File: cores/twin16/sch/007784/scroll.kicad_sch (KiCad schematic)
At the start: 90 parts, among them J1 A4H, J53 FDN, J60 R8B, J66 N8B, J75 N2B, J78 N2P, J81 R2N, K1 A4H, K80 R2P, M1 FDN, M15 FDN, M22 FDN, M29 FDN, M36 FDN, M43 FDN, M50 FDN, M57 FDN, M64 FDN, M71 FDN, M8 FDN, P1 A4H, P51 R8B, P57 FDN, P64 FDN, P71 FDN, P78 N2P, Q29 FDN, Q57 N2B, Q8 FDN

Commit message: The counter H2 is connected to FDO Q69, not counter /H2 as it was previously. The flip flop D78 for BEFLAG was incorrectly clocked, it is now clocked by the counter value for word 0 in.
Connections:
- net at J78.: now also J75.; no longer J60.
- net at O80.: now also L78.; no longer O79.
- net at P78.: now also Q57.; no longer O80.
- net at K80.: now also J81.; no longer J78.
- net at J81.: now also H79.; no longer K80.
- new net: F28. (~{R}), F70. (~{R}), F78. (~{R}), F86. (~{R}), G82. (~{R}), G82. (~{R}), G82. (~{R}), G82. (~{R}), R63.
- new net: E28. (S4), F70. (~{R})
- new net: F70. (~{R}), F70. (~{R}), F70. (~{R}), F70. (~{R}), F70. (~{R}), F70. (~{R}), F70. (~{R}), F70. (~{R}), R59.
- new net: F70. (~{R}), I21. (S4) (x4)
- new net: F70. (~{R}), F70. (~{R}), F70. (~{R}), F70. (~{R}), F70. (~{R}), F70. (~{R}), F70. (~{R}), F70. (~{R}), R17.
- new net: F70. (~{R}), P1. (S4) (x8)
- new net: J60., J78.
- new net: G21. (S4), G82. (~{R}) (x4)
- new net: E28. (S4), G21. (S4)
- new net: G21. (S4), J1. (S4)
- new net: E28. (S4), F78. (~{R})
- new net: O79., O80.
- new net: O80., P78.
- new net: L71. (~{R}), L71. (~{R}), L71. (~{R}), L71. (~{R}), L71. (~{R}), L71. (~{R}), L71. (~{R}), L71. (~{R}), R21.
- new net: J1. (S4), L71. (~{R}) (x4)
- new net: F70. (~{R}), K1. (S4) (x4)
- new net: J78., K80.
- new net: K1. (S4), L71. (~{R}) (x4)
- new net: P51., P78.
- new net: K80., L78.
- new net: E28. (S4), F28. (~{R})
- new net: J66., J81.
- new net: E28. (S4), F86. (~{R})
- new net: I21. (S4), P1. (S4)
- new net: P1. (S4), P1. (S4)
- new net: I21. (S4), K1. (S4)
- new net: J1. (S4), K1. (S4)
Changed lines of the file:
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@@
   (title_block
     (title "Konami 007784")
-    (date "2023-09-11")
+    (date "2023-10-23")
   )
   (junction (at 218.44 53.34) (diameter 0) (color 0 0 0 0)

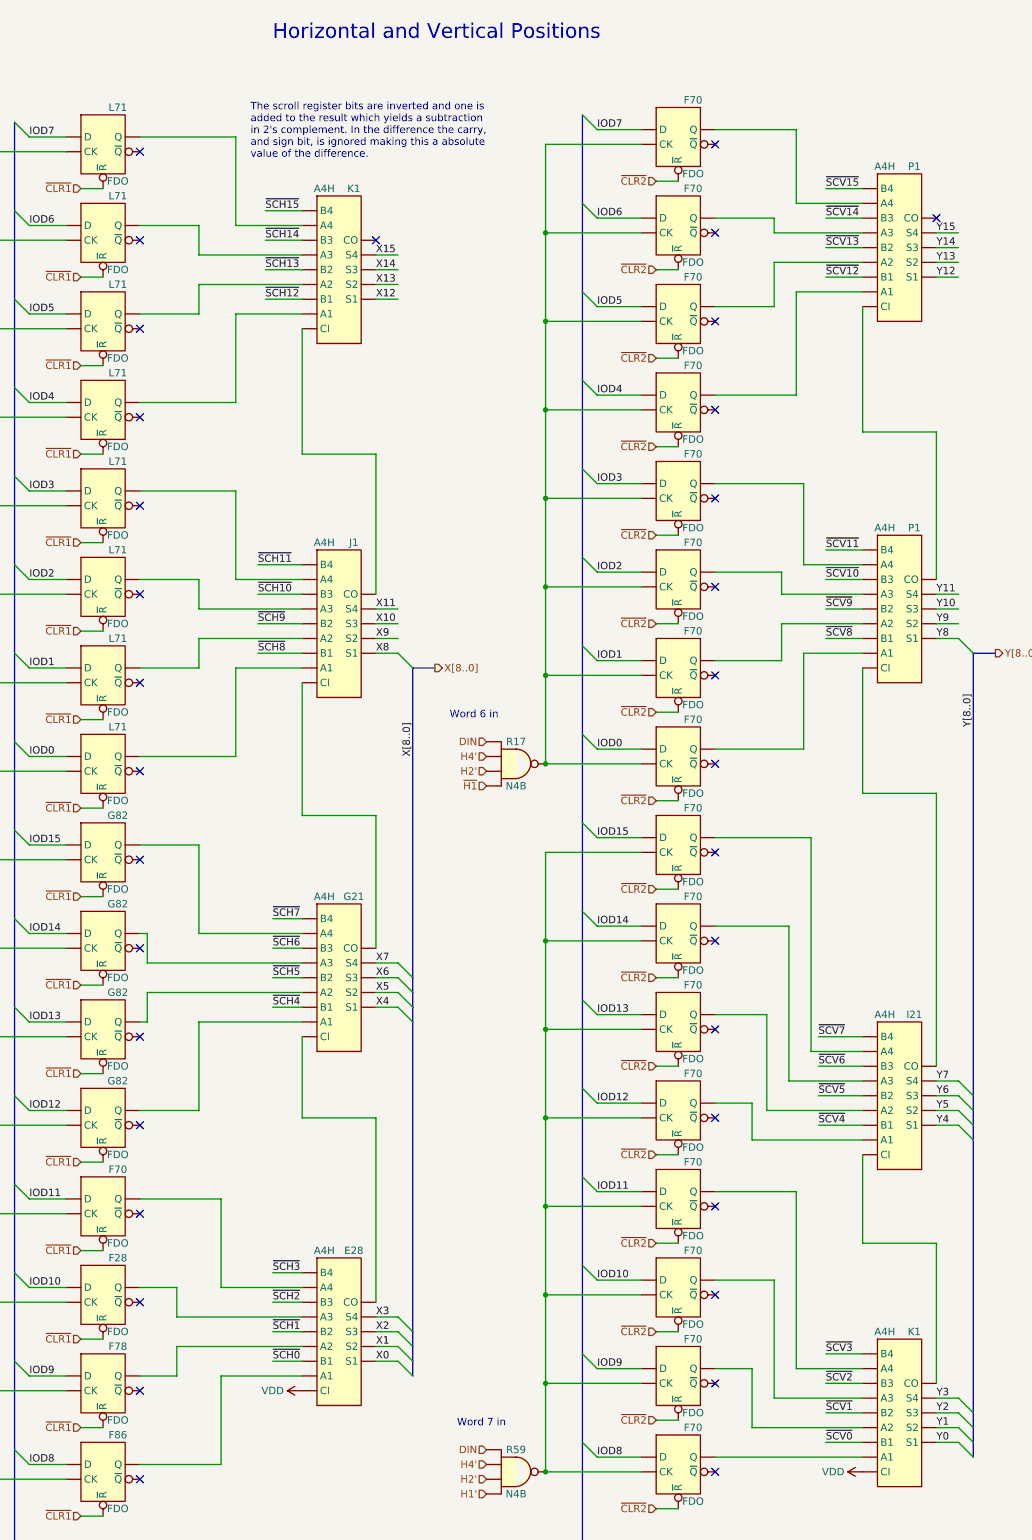
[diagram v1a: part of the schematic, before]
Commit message: updated references to jtkicad libraries
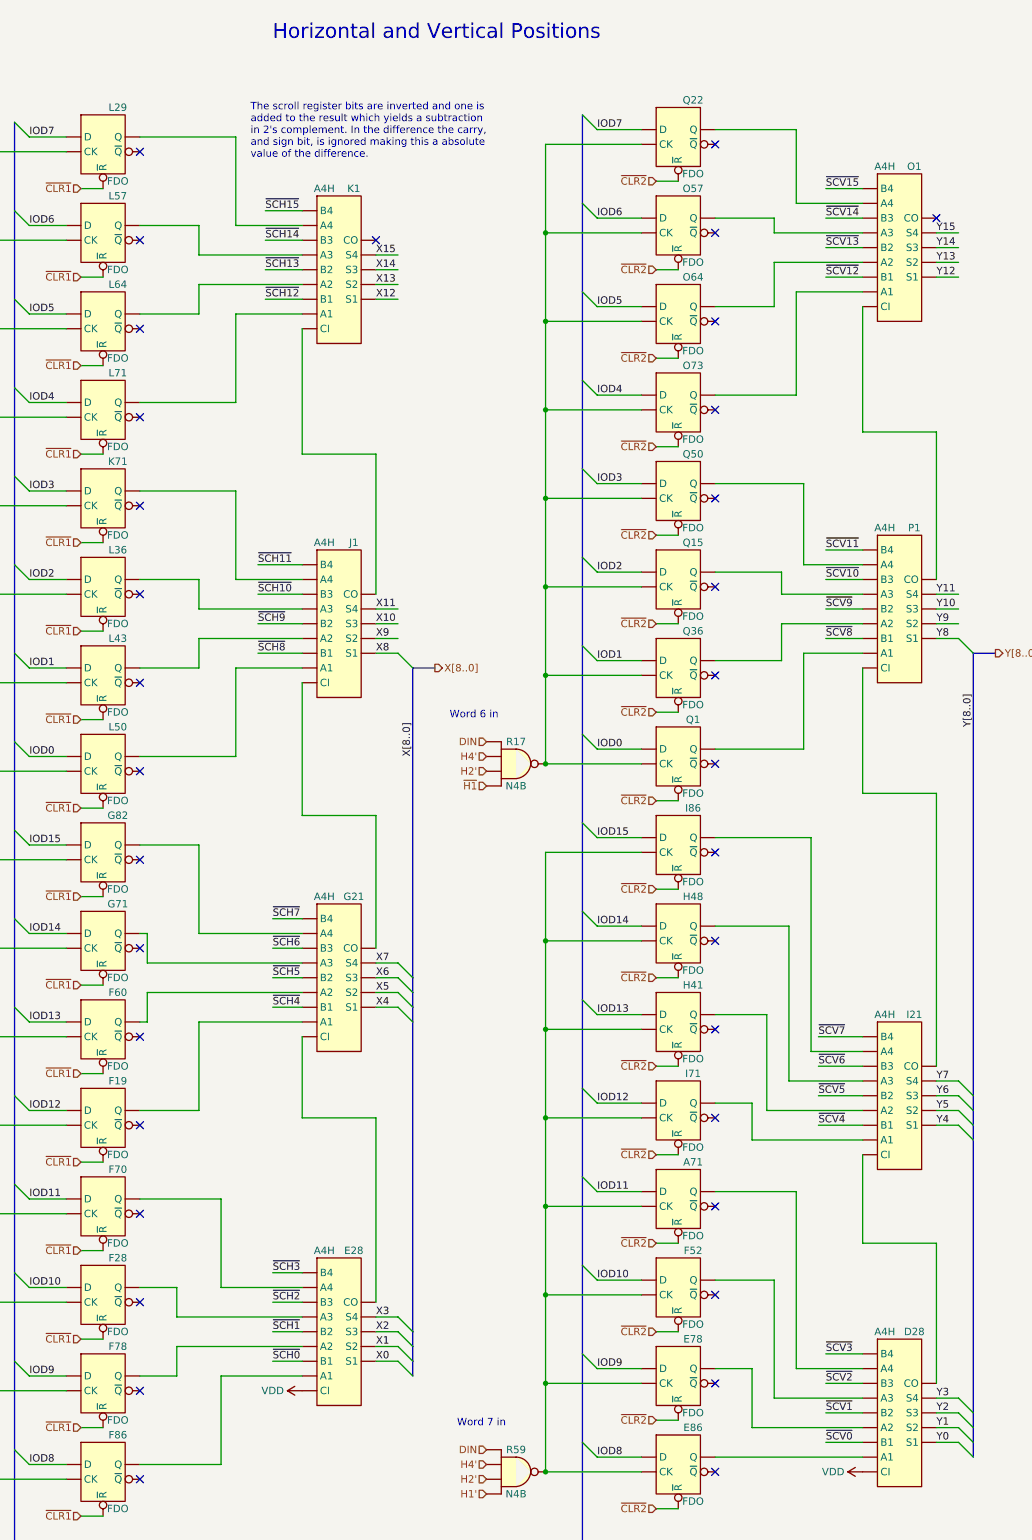
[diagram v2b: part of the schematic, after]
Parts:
- A71, E78, E86, F52, H41, H48, I71, I86, O57, O64, O73, Q1, Q15, Q22, Q36, Q50: renamed from F70; symbol fujitsu-av:FDO -> ga_fujitsu_av:FDO
- D28: renamed from K1; symbol fujitsu-av:A4H -> ga_fujitsu_av:A4H
- E28, G21, I21, J1, K1, P1: symbol fujitsu-av:A4H -> ga_fujitsu_av:A4H
- F19, F60, G71: renamed from G82; symbol fujitsu-av:FDO -> ga_fujitsu_av:FDO
- F28, F70, F78, F86, G82, L71: symbol fujitsu-av:FDO -> ga_fujitsu_av:FDO
- H79, J81: symbol fujitsu-av:R2N -> ga_fujitsu_av:R2N
- J53, L1, L15, L22, L8, M1, M15, M22, M29, M36, M43, M50, M57, M64, M71, M8, N1, N15, N22, N29, N36, N43, N50, N57, N64, N71, N8, P57, P64, P71, Q29, Q8: symbol fujitsu-av:FDN -> ga_fujitsu_av:FDN
- J60, P51: symbol fujitsu-av:R8B -> ga_fujitsu_av:R8B
- J66, O51: symbol fujitsu-av:N8B -> ga_fujitsu_av:N8B
- J75, Q57: symbol fujitsu-av:N2B -> ga_fujitsu_av:N2B
- J78, L78, P78: symbol fujitsu-av:N2P -> ga_fujitsu_av:N2P
- K71, L29, L36, L43, L50, L57, L64: renamed from L71; symbol fujitsu-av:FDO -> ga_fujitsu_av:FDO
- K80, O80: symbol fujitsu-av:R2P -> ga_fujitsu_av:R2P
- O1: renamed from P1; symbol fujitsu-av:A4H -> ga_fujitsu_av:A4H
- O79: symbol fujitsu-av:V1N -> ga_fujitsu_av:V1N
- R17, R21, R59, R63: symbol fujitsu-av:N4B -> ga_fujitsu_av:N4B
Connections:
- net at J78.: now also J75.; no longer J60.
- net at O80.: now also L78.; no longer O79.
- net at P78.: now also Q57.; no longer O80.
- net at K80.: now also J81.; no longer J78.
- net at J81.: now also H79.; no longer K80.
- new net: F19. (~{R}), F28. (~{R}), F60. (~{R}), F70. (~{R}), F78. (~{R}), F86. (~{R}), G71. (~{R}), G82. (~{R}), R63.
- new net: E28. (S4), F70. (~{R})
- new net: A71. (~{R}), E78. (~{R}), E86. (~{R}), F52. (~{R}), H41. (~{R}), H48. (~{R}), I71. (~{R}), I86. (~{R}), R59.
- new net: I21. (S4), I71. (~{R})
- new net: O57. (~{R}), O64. (~{R}), O73. (~{R}), Q1. (~{R}), Q15. (~{R}), Q22. (~{R}), Q36. (~{R}), Q50. (~{R}), R17.
- new net: P1. (S4), Q36. (~{R})
- new net: J60., J78.
- new net: F19. (~{R}), G21. (S4)
- new net: E28. (S4), G21. (S4)
- new net: G21. (S4), G82. (~{R})
- new net: F60. (~{R}), G21. (S4)
- new net: G21. (S4), G71. (~{R})
- new net: G21. (S4), J1. (S4)
- new net: E28. (S4), F78. (~{R})
- new net: O1. (S4), O57. (~{R})
- new net: O79., O80.
- new net: O80., P78.
- new net: K71. (~{R}), L29. (~{R}), L36. (~{R}), L43. (~{R}), L50. (~{R}), L57. (~{R}), L64. (~{R}), L71. (~{R}), R21.
- new net: J1. (S4), L50. (~{R})
- new net: J1. (S4), L43. (~{R})
- new net: A71. (~{R}), D28. (S4)
- new net: J78., K80.
- new net: H41. (~{R}), I21. (S4)
- new net: K1. (S4), L64. (~{R})
- new net: P1. (S4), Q50. (~{R})
- new net: K1. (S4), L57. (~{R})
- new net: D28. (S4), E86. (~{R})
- new net: P51., P78.
- new net: K80., L78.
- new net: E28. (S4), F28. (~{R})
- new net: K1. (S4), L71. (~{R})
- new net: D28. (S4), F52. (~{R})
- new net: J66., J81.
- new net: E28. (S4), F86. (~{R})
- new net: P1. (S4), Q15. (~{R})
- new net: P1. (S4), Q1. (~{R})
- new net: J1. (S4), K71. (~{R})
- new net: O1. (S4), O64. (~{R})
- new net: K1. (S4), L29. (~{R})
- new net: I21. (S4), P1. (S4)
- new net: O1. (S4), P1. (S4)
- new net: I21. (S4), I86. (~{R})
- new net: D28. (S4), E78. (~{R})
- new net: O1. (S4), Q22. (~{R})
- new net: D28. (S4), I21. (S4)
- new net: O1. (S4), O73. (~{R})
- new net: J1. (S4), L36. (~{R})
- new net: H48. (~{R}), I21. (S4)
- new net: J1. (S4), K1. (S4)

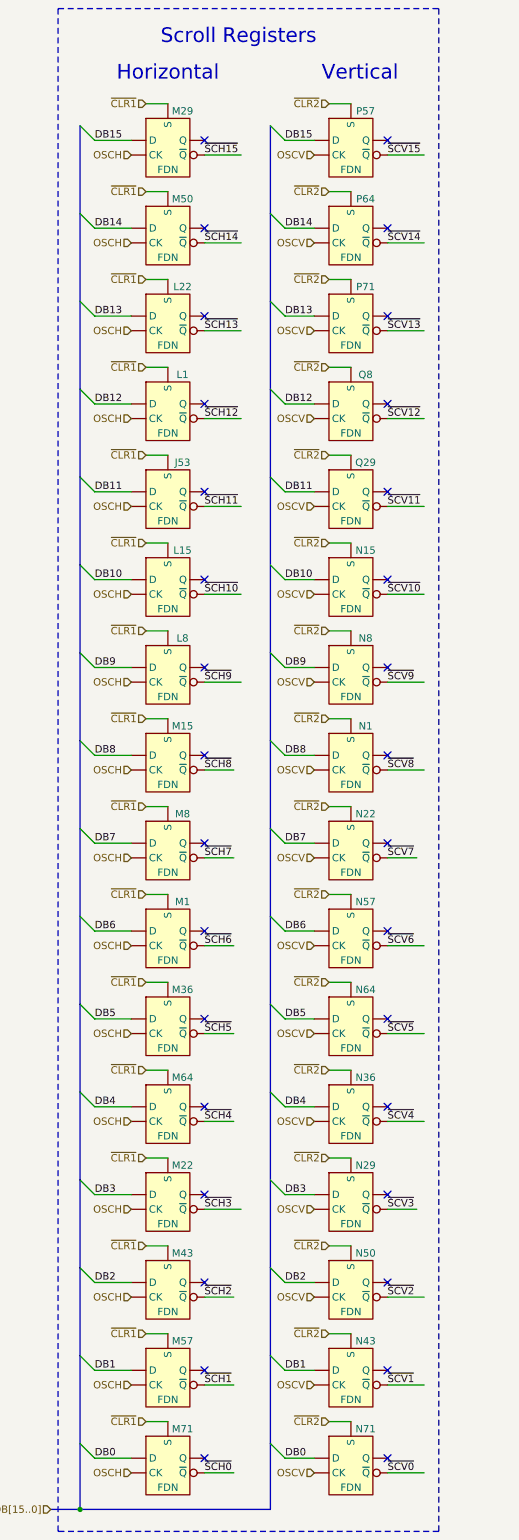
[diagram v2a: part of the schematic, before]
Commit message: changed symbol FDN to active low symbol. Updated to correct name for OKI Gate Arrays.
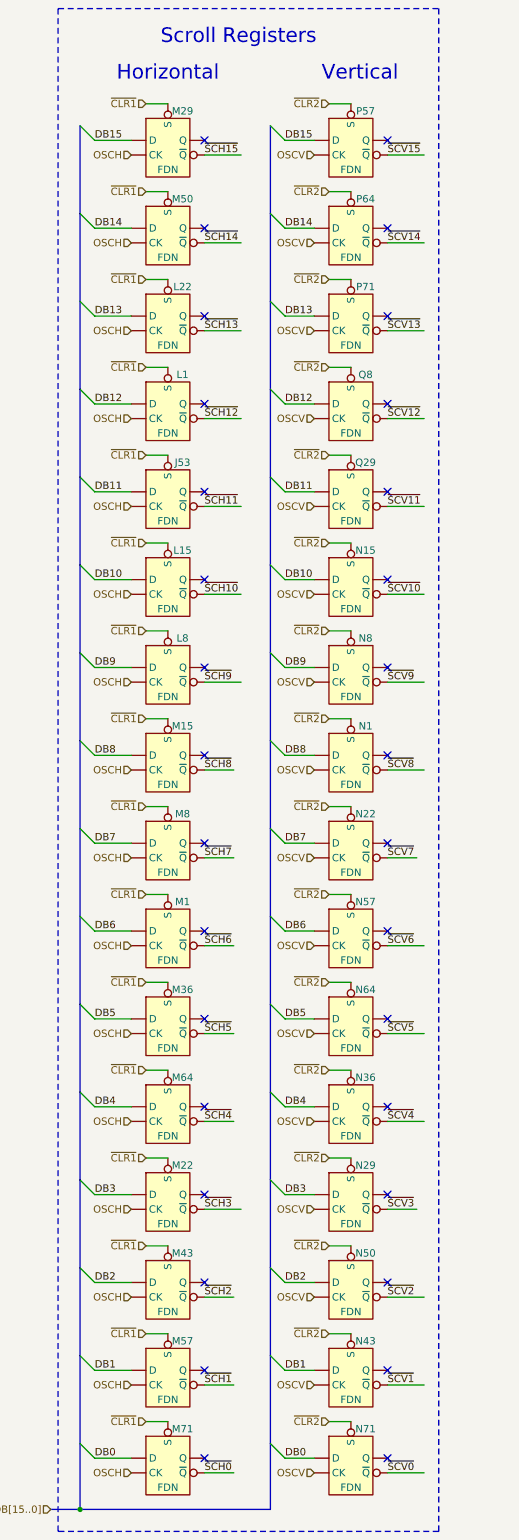
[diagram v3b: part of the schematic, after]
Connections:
- net at J78.: now also J75.; no longer J60.
- net at O80.: now also L78.; no longer O79.
- net at P78.: now also Q57.; no longer O80.
- net at K80.: now also J81.; no longer J78.
- net at J81.: now also H79.; no longer K80.
- new net: F19. (~{R}), F28. (~{R}), F60. (~{R}), F70. (~{R}), F78. (~{R}), F86. (~{R}), G71. (~{R}), G82. (~{R}), R63.
- new net: E28. (S4), F70. (~{R})
- new net: A71. (~{R}), E78. (~{R}), E86. (~{R}), F52. (~{R}), H41. (~{R}), H48. (~{R}), I71. (~{R}), I86. (~{R}), R59.
- new net: I21. (S4), I71. (~{R})
- new net: O57. (~{R}), O64. (~{R}), O73. (~{R}), Q1. (~{R}), Q15. (~{R}), Q22. (~{R}), Q36. (~{R}), Q50. (~{R}), R17.
- new net: P1. (S4), Q36. (~{R})
- new net: J60., J78.
- new net: F19. (~{R}), G21. (S4)
- new net: E28. (S4), G21. (S4)
- new net: G21. (S4), G82. (~{R})
- new net: F60. (~{R}), G21. (S4)
- new net: G21. (S4), G71. (~{R})
- new net: G21. (S4), J1. (S4)
- new net: E28. (S4), F78. (~{R})
- new net: O1. (S4), O57. (~{R})
- new net: O79., O80.
- new net: O80., P78.
- new net: K71. (~{R}), L29. (~{R}), L36. (~{R}), L43. (~{R}), L50. (~{R}), L57. (~{R}), L64. (~{R}), L71. (~{R}), R21.
- new net: J1. (S4), L50. (~{R})
- new net: J1. (S4), L43. (~{R})
- new net: A71. (~{R}), D28. (S4)
- new net: J78., K80.
- new net: H41. (~{R}), I21. (S4)
- new net: K1. (S4), L64. (~{R})
- new net: P1. (S4), Q50. (~{R})
- new net: K1. (S4), L57. (~{R})
- new net: D28. (S4), E86. (~{R})
- new net: P51., P78.
- new net: K80., L78.
- new net: E28. (S4), F28. (~{R})
- new net: K1. (S4), L71. (~{R})
- new net: D28. (S4), F52. (~{R})
- new net: J66., J81.
- new net: E28. (S4), F86. (~{R})
- new net: P1. (S4), Q15. (~{R})
- new net: P1. (S4), Q1. (~{R})
- new net: J1. (S4), K71. (~{R})
- new net: O1. (S4), O64. (~{R})
- new net: K1. (S4), L29. (~{R})
- new net: I21. (S4), P1. (S4)
- new net: O1. (S4), P1. (S4)
- new net: I21. (S4), I86. (~{R})
- new net: D28. (S4), E78. (~{R})
- new net: O1. (S4), Q22. (~{R})
- new net: D28. (S4), I21. (S4)
- new net: O1. (S4), O73. (~{R})
- new net: J1. (S4), L36. (~{R})
- new net: H48. (~{R}), I21. (S4)
- new net: J1. (S4), K1. (S4)

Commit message: twin16 - wip - sch labels
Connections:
- net at J78.: now also J75.; no longer J60.
- net at O80.: now also L78.; no longer O79.
- net at P78.: now also Q57.; no longer O80.
- net at K80.: now also J81.; no longer J78.
- net at J81.: now also H79.; no longer K80.
- new net: F19. (~{R}), F28. (~{R}), F60. (~{R}), F70. (~{R}), F78. (~{R}), F86. (~{R}), G71. (~{R}), G82. (~{R}), R63.
- new net: E28. (S4), F70. (~{R})
- new net: A71. (~{R}), E78. (~{R}), E86. (~{R}), F52. (~{R}), H41. (~{R}), H48. (~{R}), I71. (~{R}), I86. (~{R}), R59.
- new net: I21. (S4), I71. (~{R})
- new net: O57. (~{R}), O64. (~{R}), O73. (~{R}), Q1. (~{R}), Q15. (~{R}), Q22. (~{R}), Q36. (~{R}), Q50. (~{R}), R17.
- new net: P1. (S4), Q36. (~{R})
- new net: J60., J78.
- new net: F19. (~{R}), G21. (S4)
- new net: E28. (S4), G21. (S4)
- new net: G21. (S4), G82. (~{R})
- new net: F60. (~{R}), G21. (S4)
- new net: G21. (S4), G71. (~{R})
- new net: G21. (S4), J1. (S4)
- new net: E28. (S4), F78. (~{R})
- new net: O1. (S4), O57. (~{R})
- new net: O79., O80.
- new net: O80., P78.
- new net: K71. (~{R}), L29. (~{R}), L36. (~{R}), L43. (~{R}), L50. (~{R}), L57. (~{R}), L64. (~{R}), L71. (~{R}), R21.
- new net: J1. (S4), L50. (~{R})
- new net: J1. (S4), L43. (~{R})
- new net: A71. (~{R}), D28. (S4)
- new net: J78., K80.
- new net: H41. (~{R}), I21. (S4)
- new net: K1. (S4), L64. (~{R})
- new net: P1. (S4), Q50. (~{R})
- new net: K1. (S4), L57. (~{R})
- new net: D28. (S4), E86. (~{R})
- new net: P51., P78.
- new net: K80., L78.
- new net: E28. (S4), F28. (~{R})
- new net: K1. (S4), L71. (~{R})
- new net: D28. (S4), F52. (~{R})
- new net: J66., J81.
- new net: E28. (S4), F86. (~{R})
- new net: P1. (S4), Q15. (~{R})
- new net: P1. (S4), Q1. (~{R})
- new net: J1. (S4), K71. (~{R})
- new net: O1. (S4), O64. (~{R})
- new net: K1. (S4), L29. (~{R})
- new net: I21. (S4), P1. (S4)
- new net: O1. (S4), P1. (S4)
- new net: I21. (S4), I86. (~{R})
- new net: D28. (S4), E78. (~{R})
- new net: O1. (S4), Q22. (~{R})
- new net: D28. (S4), I21. (S4)
- new net: O1. (S4), O73. (~{R})
- new net: J1. (S4), L36. (~{R})
- new net: H48. (~{R}), I21. (S4)
- new net: J1. (S4), K1. (S4)
